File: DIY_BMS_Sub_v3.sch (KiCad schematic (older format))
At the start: 40 parts, among them J1 Conn_01x11, J2 Conn_02x04_Top_Bottom, J3 Conn_02x03_Top_Bottom, J4 Conn_02x03_Top_Bottom, SW1 SW_DIP_x04, U1 BQ76PL536A

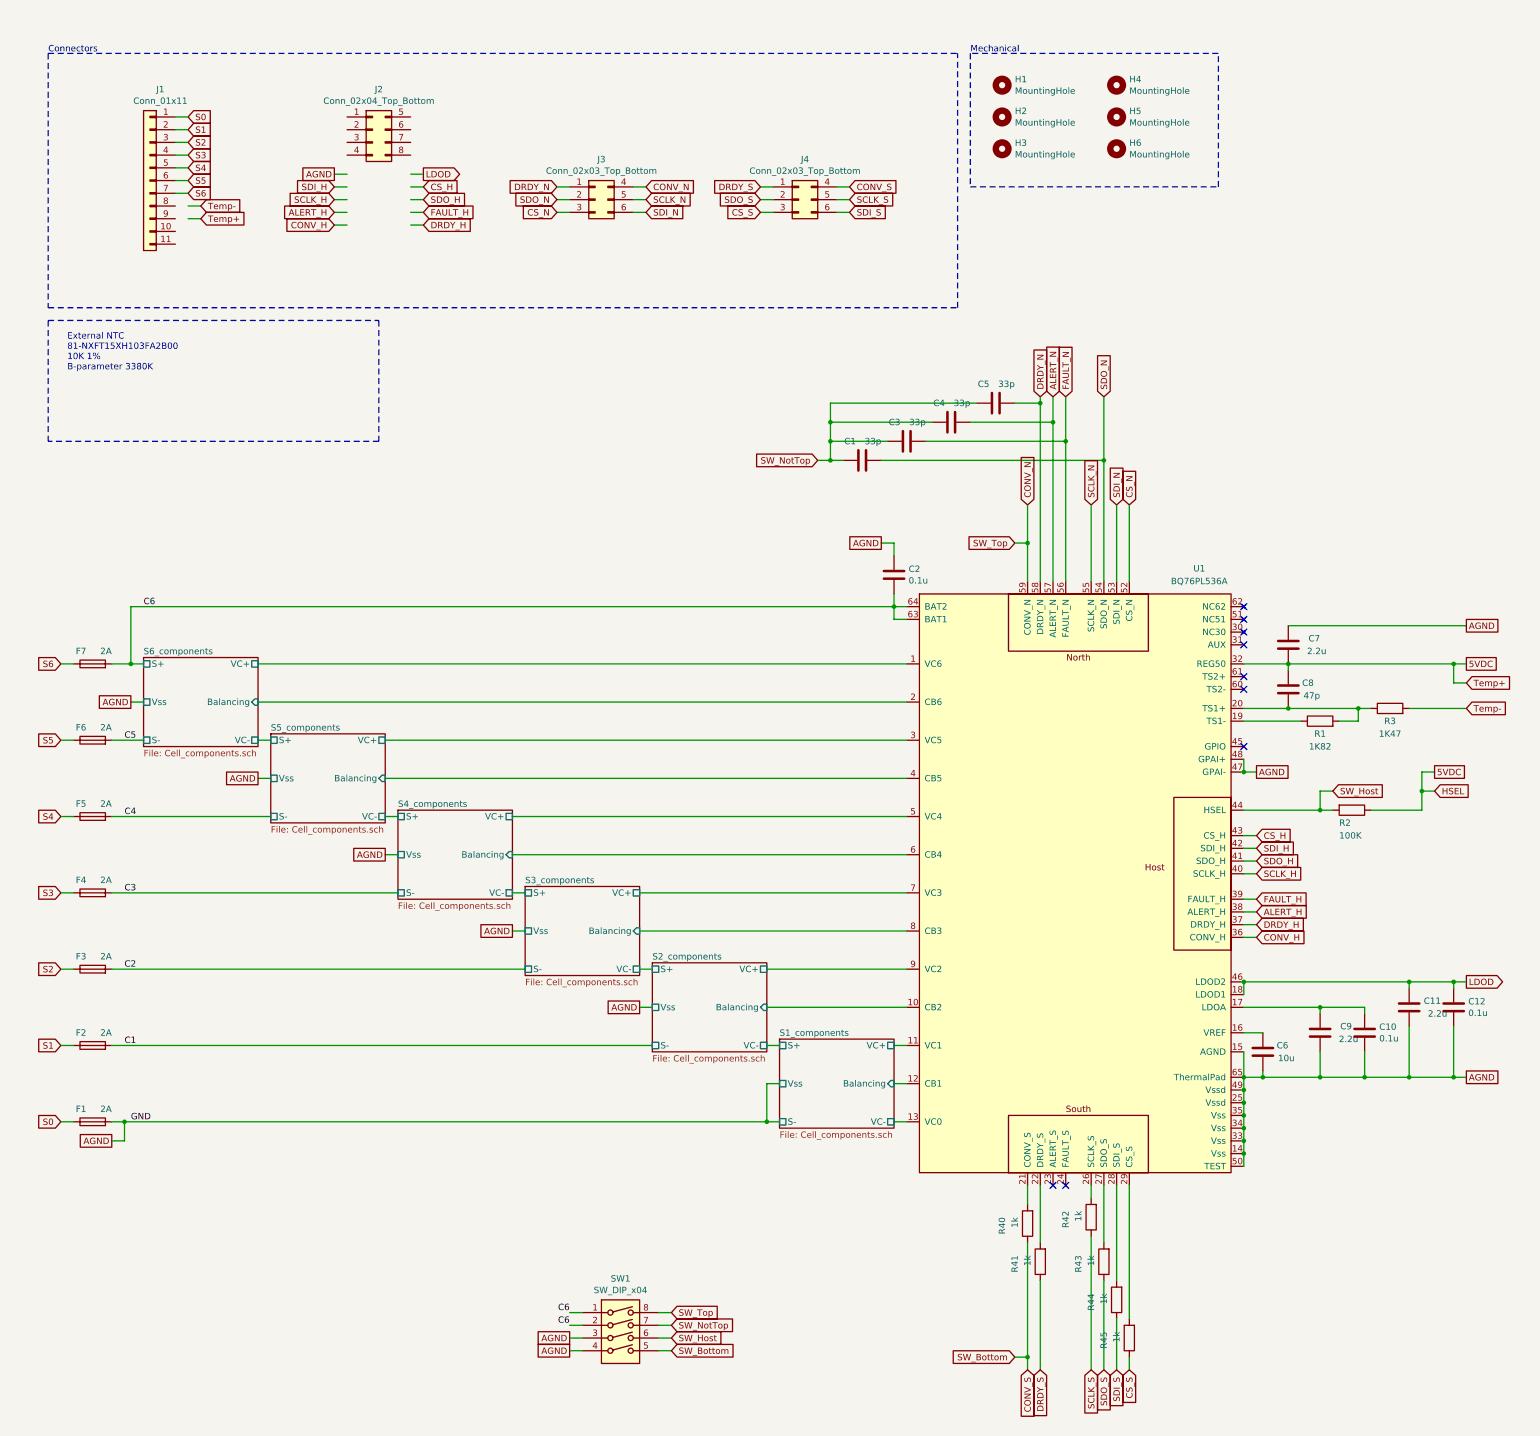
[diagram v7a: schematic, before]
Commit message: Add files via upload
Routed external thermistor and HOST-interface traces. Added silkscreen text. Placed additional AGND-via's.
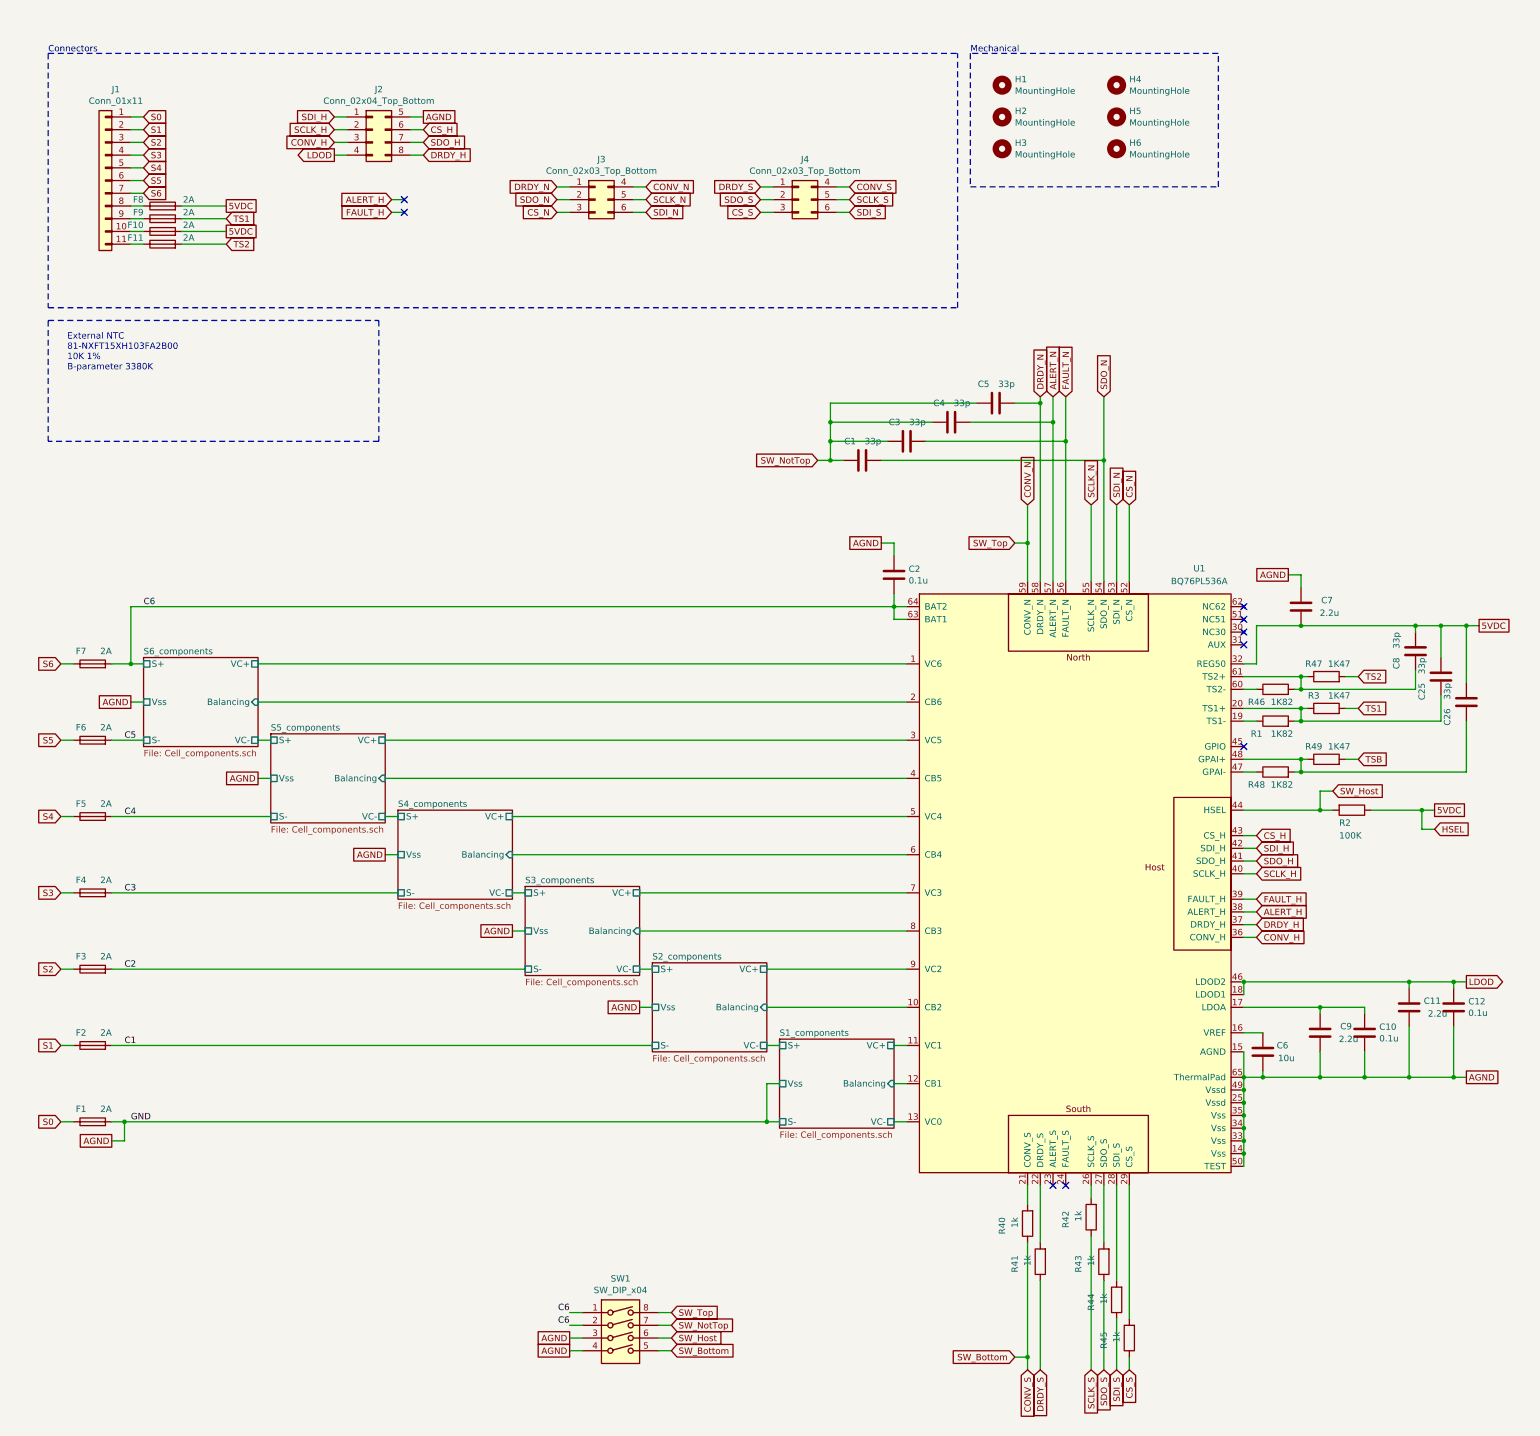
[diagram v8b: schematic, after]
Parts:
- added C25, C26: 33p, Capacitor_SMD:C_0603_1608Metric_Pad1.05x0.95mm_HandSolder, symbol Device:C
- added F10, F11, F8, F9: 2A, Fuse:Fuse_0603_1608Metric_Pad1.05x0.95mm_HandSolder, symbol Device:Fuse
- added R46, R48: 1K82, Resistor_SMD:R_0603_1608Metric_Pad1.05x0.95mm_HandSolder, symbol Device:R
- added R47, R49: 1K47, Resistor_SMD:R_0603_1608Metric_Pad1.05x0.95mm_HandSolder, symbol Device:R
- C8: value 47p -> 33p; footprint Capacitor_SMD:C_0805_2012Metric_Pad1.15x1.40mm_HandSolder -> Capacitor_SMD:C_0603_1608Metric_Pad1.05x0.95mm_HandSolder; LCSC C14857 -> C1663
- U1: footprint Package_QFP:HTQFP-64-1EP_10x10mm_P0.5mm_EP8x8mm_Mask4.4x4.4mm_ThermalVias -> #_custom_footprints:HTQFP-64-1EP_10x10mm_P0.5mm_EP8x8mm_Mask4.4x4.4mm_LessThermalVias
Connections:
- net labels added: TS1, TS2, TSB
- net labels removed: Temp+, Temp-
- wire segments 194 -> 219
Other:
- moved on the sheet: C7, J1, R1, R3
